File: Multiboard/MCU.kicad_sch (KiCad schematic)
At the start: 50 parts, among them J1 Conn_01x20_Socket, J2 Conn_01x20_Socket, J3 Debug, J4 USB_C_Receptacle_USB2.0_16P, SW1 BOOT0, SW2 NRST, SW7 KEY, U1 STM32F411RET6, U2 MAX662AESA_T, U3 MCP1792x-3302xCB, Y1 32.768KHz, Y2 25MHz

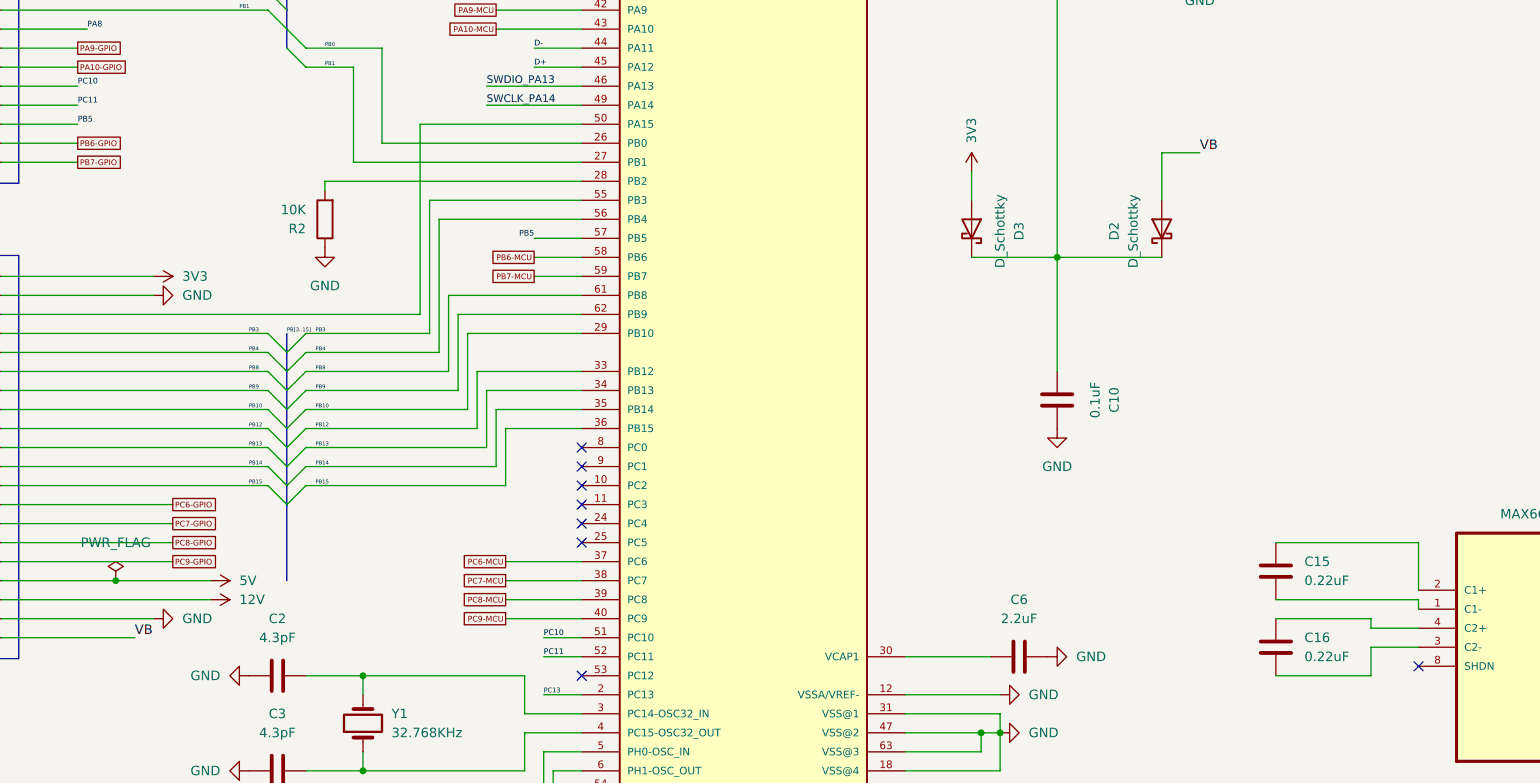
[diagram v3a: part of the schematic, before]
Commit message: positioned and wired FTDI
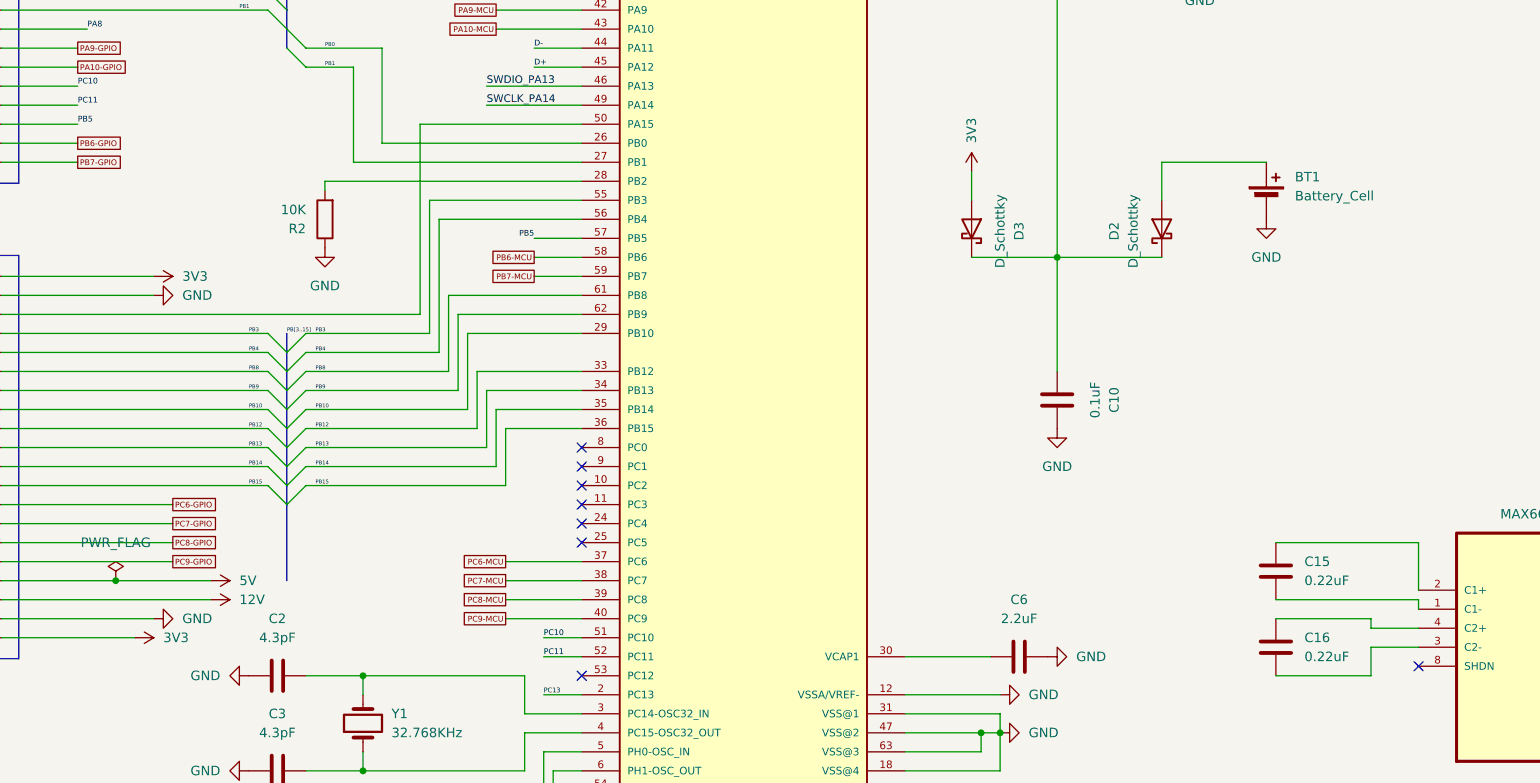
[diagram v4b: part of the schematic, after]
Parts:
- added BT1: Battery_Cell, Battery:Battery_Panasonic_CR2032-VS1N_Vertical_CircularHoles, symbol Device:Battery_Cell
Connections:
- net 3V3: now also J2.20 (Pin_20)
- net GND: now also BT1.2 (-)
- net VB: no longer names the net of D2.2 (A)
- net VB: now also BT1.1 (+); no longer J2.20 (Pin_20)
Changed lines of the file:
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@@
 	(wire
 		(pts
-			(xy 233.68 109.22) (xy 233.68 115.57)
+			(xy 233.68 110.49) (xy 233.68 115.57)
 		)
 		(stroke
@@
 	(wire
 		(pts
-			(xy 238.76 109.22) (xy 233.68 109.22)
+			(xy 233.68 110.49) (xy 247.65 110.49)
 		)
 		(stroke
@@
 		)
 	)
-	(label "VB"
-		(at 238.76 109.22 0)
-		(effects
-			(font
-				(size 1.27 1.27)
-			)
-			(justify left bottom)
-		)
-	)
 	(label "PC13"
 		(at 280.67 22.86 0)
@@
 		)
 	)
-	(label "VB"
-		(at 96.52 173.99 0)
-		(effects
-			(font
-				(size 1.27 1.27)
-			)
-			(justify left bottom)
-		)
-	)
 	(label "PB12"
 		(at 111.76 146.05 0)
@@
 	)
 	(symbol
+		(lib_id "power:VCC")
+		(at 96.52 173.99 270)
+		(unit 1)
+		(exclude_from_sim no)
+		(in_bom yes)
+		(on_board yes)
+		(dnp no)
+		(fields_autoplaced yes)
+		(property "Reference" "#PWR0139"
+			(at 92.71 173.99 0)
+			(effects
+				(font
+					(size 1.27 1.27)
+				)
+				(hide yes)
+			)
+		)
+		(property "Value" "3V3"
+			(at 100.33 173.9899 90)
+			(effects
+				(font
+					(size 1.27 1.27)
+				)
+				(justify left)
+			)
+		)
+		(property "Footprint" ""
+			(at 96.52 173.99 0)
+			(effects
+				(font
+					(size 1.27 1.27)
+				)
+				(hide yes)
+			)
+		)
+		(property "Datasheet" ""
+			(at 96.52 173.99 0)
+			(effects
+				(font
+					(size 1.27 1.27)
+				)
+				(hide yes)
+			)
+		)
+		(property "Description" "Power symbol creates a global label with name \"VCC\""
+			(at 96.52 173.99 0)
+			(effects
+				(font
+					(size 1.27 1.27)
+				)
+				(hide yes)
+			)
+		)
+		(pin "1"
+		)
+		(instances
+			(project "Multiboard"
+				(path "/9ed4a389-3aa7-41f1-b239-280eb7f09ef1/2bca3eb5-73b3-4aa8-9f30-e1743a374253"
+					(reference "#PWR0139")
+					(unit 1)
+				)
+			)
+		)
+	)
+	(symbol
 		(lib_id "Device:D_Schottky")
 		(at 208.28 119.38 270)
@@
 	)
 	(symbol
+		(lib_id "power:GND")
+		(at 247.65 118.11 0)
+		(unit 1)
+		(exclude_from_sim no)
+		(in_bom yes)
+		(on_board yes)
+		(dnp no)
+		(fields_autoplaced yes)
+		(property "Reference" "#PWR0123"
+			(at 247.65 124.46 0)
+			(effects
+				(font
+					(size 1.27 1.27)
+				)
+				(hide yes)
+			)
+		)
+		(property "Value" "GND"
+			(at 247.65 123.19 0)
+			(effects
+				(font
+					(size 1.27 1.27)
+				)
+			)
+		)
+		(property "Footprint" ""
+			(at 247.65 118.11 0)
+			(effects
+				(font
+					(size 1.27 1.27)
+				)
+				(hide yes)
+			)
+		)
+		(property "Datasheet" ""
+			(at 247.65 118.11 0)
+			(effects
+				(font
+					(size 1.27 1.27)
+				)
+				(hide yes)
+			)
+		)
+		(property "Description" "Power symbol creates a global label with name \"GND\" , ground"
+			(at 247.65 118.11 0)
+			(effects
+				(font
+					(size 1.27 1.27)
+				)
+				(hide yes)
+			)
+		)
+		(pin "1"
+		)
+		(instances
+			(project "Multiboard"
+				(path "/9ed4a389-3aa7-41f1-b239-280eb7f09ef1/2bca3eb5-73b3-4aa8-9f30-e1743a374253"
+					(reference "#PWR0123")
+					(unit 1)
+				)
+			)
+		)
+	)
+	(symbol
 		(lib_id "Connector:Conn_01x20_Socket")
 		(at 73.66 148.59 0)
@@
 					(unit 1)
 				)
+			)
+		)
+	)
+	(symbol
+		(lib_id "Device:Battery_Cell")
+		(at 247.65 115.57 0)
+		(unit 1)
+		(exclude_from_sim no)
+		(in_bom yes)
+		(on_board yes)
+		(dnp no)
+		(fields_autoplaced yes)
+		(property "Reference" "BT1"
+			(at 251.46 112.4584 0)
+			(effects
+				(font
+					(size 1.27 1.27)
+				)
+				(justify left)
+			)
+		)
+		(property "Value" "Battery_Cell"
+			(at 251.46 114.9984 0)
+			(effects
+				(font
+					(size 1.27 1.27)
+				)
+				(justify left)
+			)
+		)
+		(property "Footprint" "Battery:Battery_Panasonic_CR2032-VS1N_Vertical_CircularHoles"
+			(at 247.65 114.046 90)
+			(effects
+				(font
+					(size 1.27 1.27)
+				)
+				(hide yes)
+			)
+		)
+		(property "Datasheet" "~"
+			(at 247.65 114.046 90)
+			(effects
+				(font
+					(size 1.27 1.27)
+				)
+				(hide yes)
+			)
+		)
+		(property "Description" "Single-cell battery"
+			(at 247.65 115.57 0)
+			(effects
+				(font
+					(size 1.27 1.27)
+				)
+				(hide yes)
+			)
+		)
+		(property "Sim.Device" "V"
+			(at 247.65 115.57 0)
+			(effects
+				(font
+					(size 1.27 1.27)
+				)
+				(hide yes)
+			)
+		)
+		(property "Sim.Type" "DC"
+			(at 247.65 115.57 0)
+			(effects
+				(font
+					(size 1.27 1.27)
+				)
+				(hide yes)
+			)
+		)
+		(property "Sim.Pins" "1=+ 2=-"
+			(at 247.65 115.57 0)
+			(effects
+				(font
+					(size 1.27 1.27)
+				)
+				(hide yes)
+			)
+		)
+		(pin "1"
+		)
+		(pin "2"
+		)
+		(instances
+			(project ""
+				(path "/9ed4a389-3aa7-41f1-b239-280eb7f09ef1/2bca3eb5-73b3-4aa8-9f30-e1743a374253"
+					(reference "BT1")
+					(unit 1)
+				)

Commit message: test reverse polarity
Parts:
- added D20, D21, D22: D_Schottky, symbol Device:D_Schottky
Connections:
- net 3V3: now also D20.2 (A), D22.2 (A)
- net 5V: now also D21.1 (K); no longer J1.1 (Pin_1)
- net GND: now also D20.1 (K), D22.1 (K)
- new net: D21.2 (A), J1.1 (Pin_1)
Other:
- moved on the sheet: J3

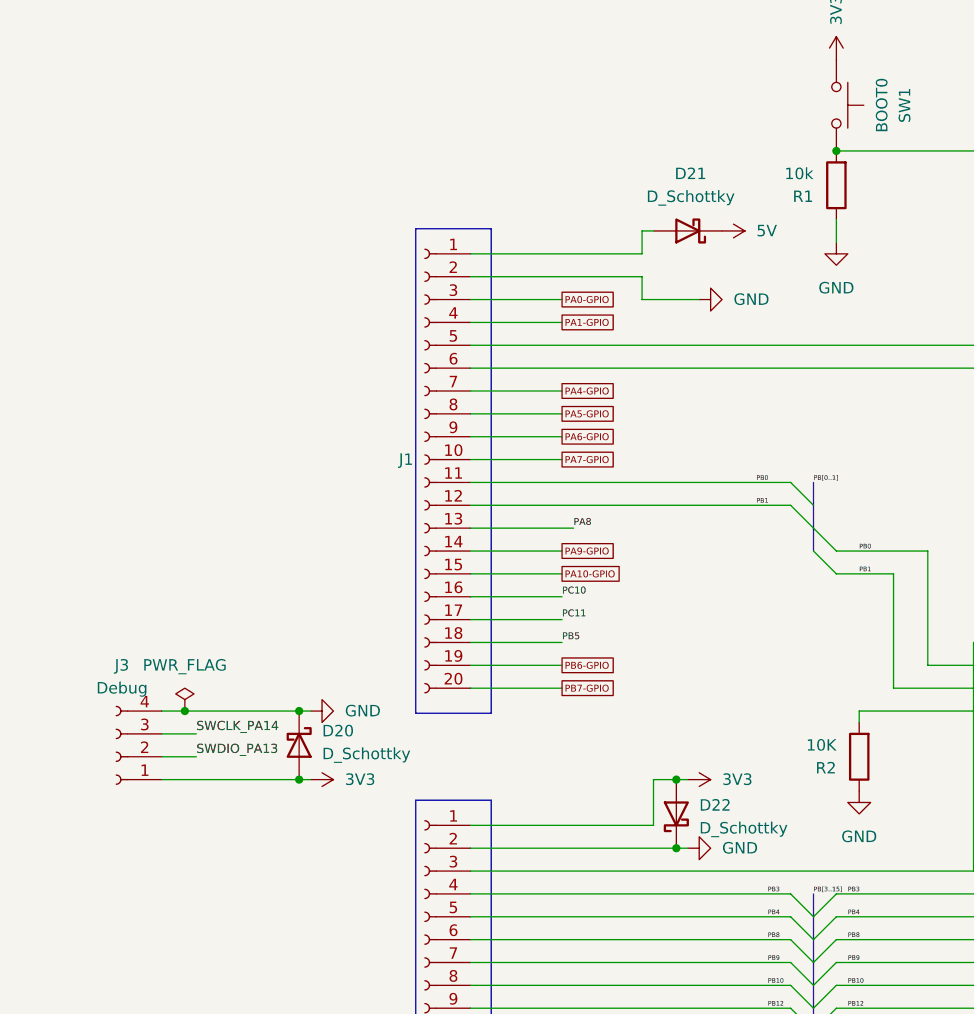
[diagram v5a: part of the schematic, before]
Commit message: wired power traces and added prototype area
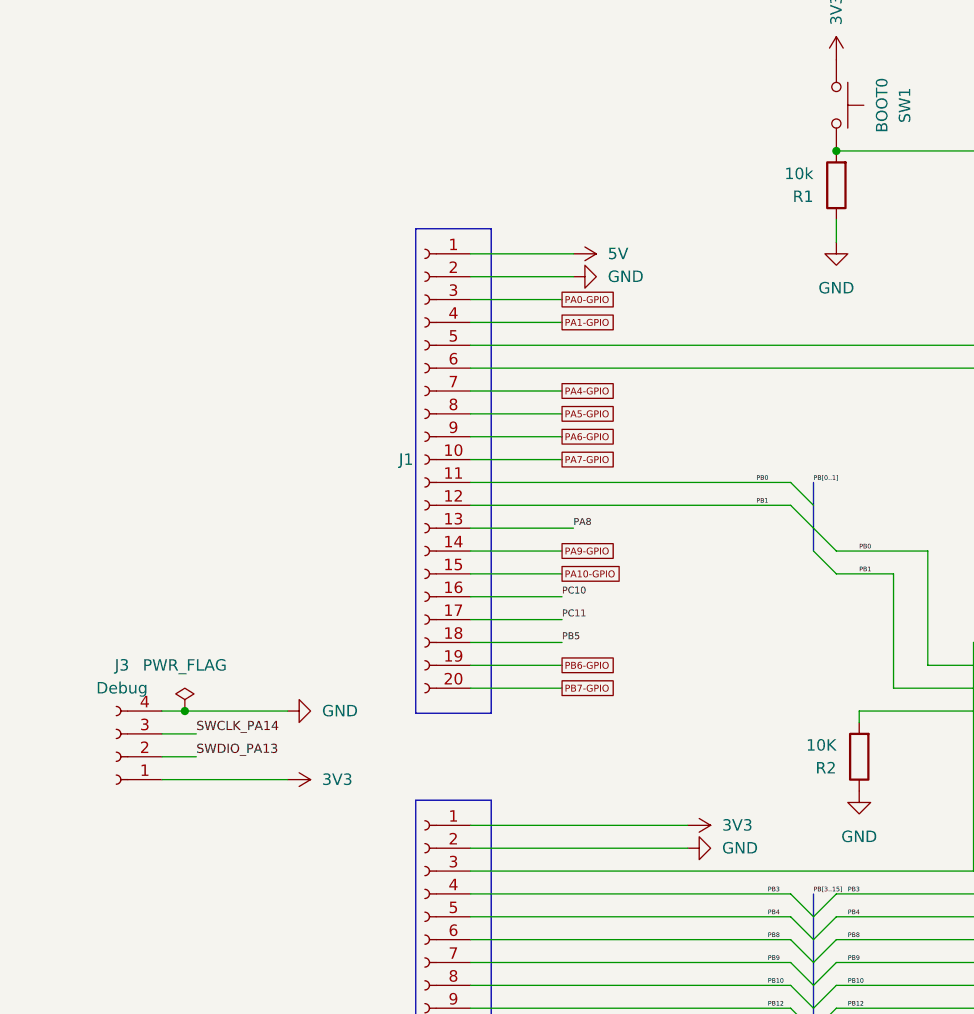
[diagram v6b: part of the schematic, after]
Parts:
- removed D20, D21, D22: D_Schottky, symbol Device:D_Schottky
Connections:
- net 5V: now also J1.1 (Pin_1)

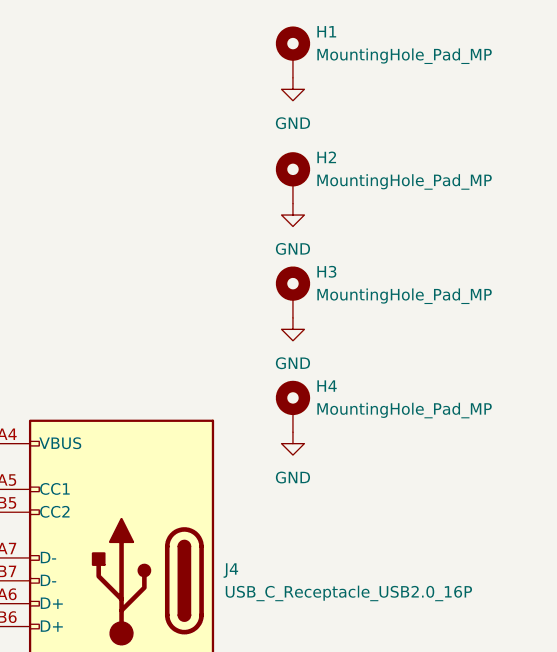
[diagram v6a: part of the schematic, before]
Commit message: fixed fpga header issue
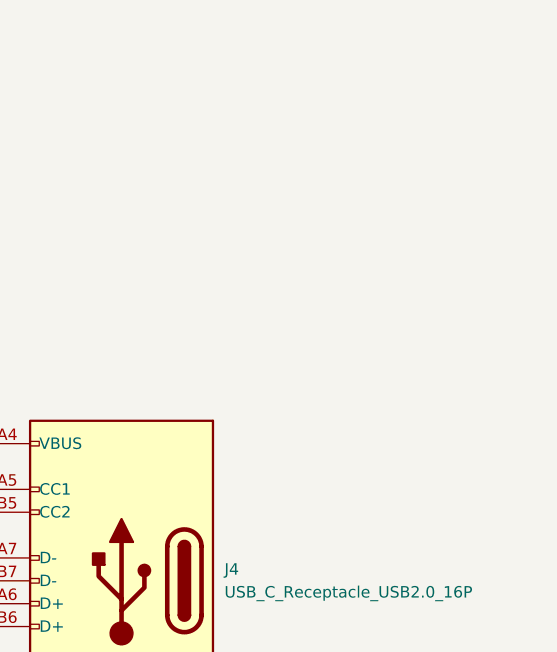
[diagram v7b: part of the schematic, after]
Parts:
- removed H1, H2, H3, H4: MountingHole_Pad_MP, MountingHole:MountingHole_3.2mm_M3_DIN965_Pad_TopBottom, symbol Mechanical:MountingHole_Pad_MP

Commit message: cleared part of errors and warnings
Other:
- company: (none) -> Technological School "Electronic Systems"
- title: (none) -> IR-Multiboard/MCU
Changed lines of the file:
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@@
 	(generator_version "9.0")
 	(paper "A3")
+	(title_block
+		(title "IR-Multiboard/MCU")
+		(date "2026-02-23")
+		(company "Technological School \"Electronic Systems\"")
+	)
 	(rectangle
 		(start 72.644 59.436)
